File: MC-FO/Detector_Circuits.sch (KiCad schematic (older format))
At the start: 9 parts, among them U16 IFD97, U17 74LVC1G32SE-7, U18 TLV3501AID

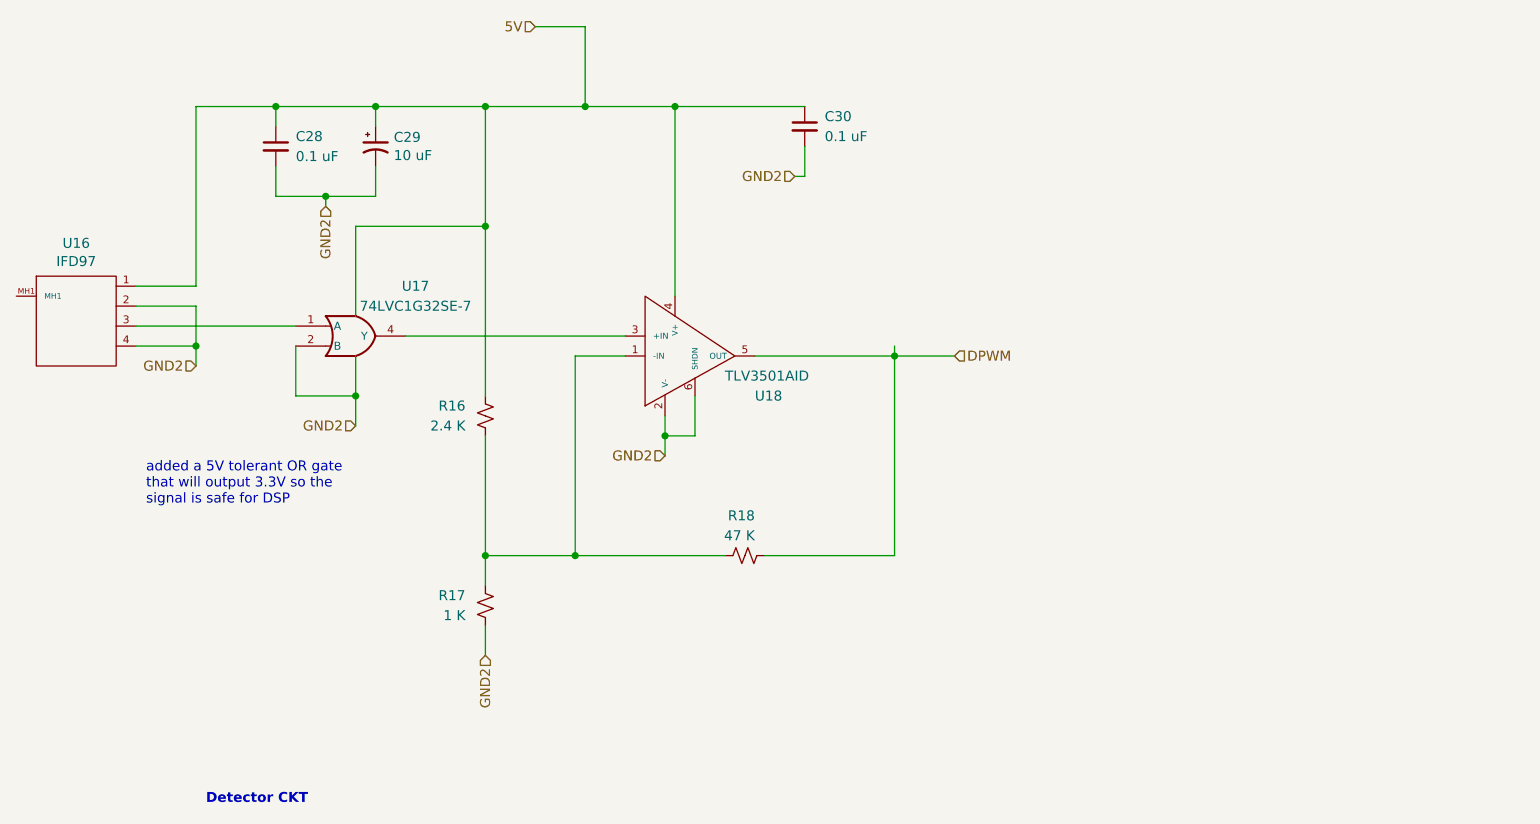
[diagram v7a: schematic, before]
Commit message: unpopulated cap after voltage regulators
and changed reference designator numbering scheme
and moved the or gate that sends 3.3 V to comparator in detector ckt
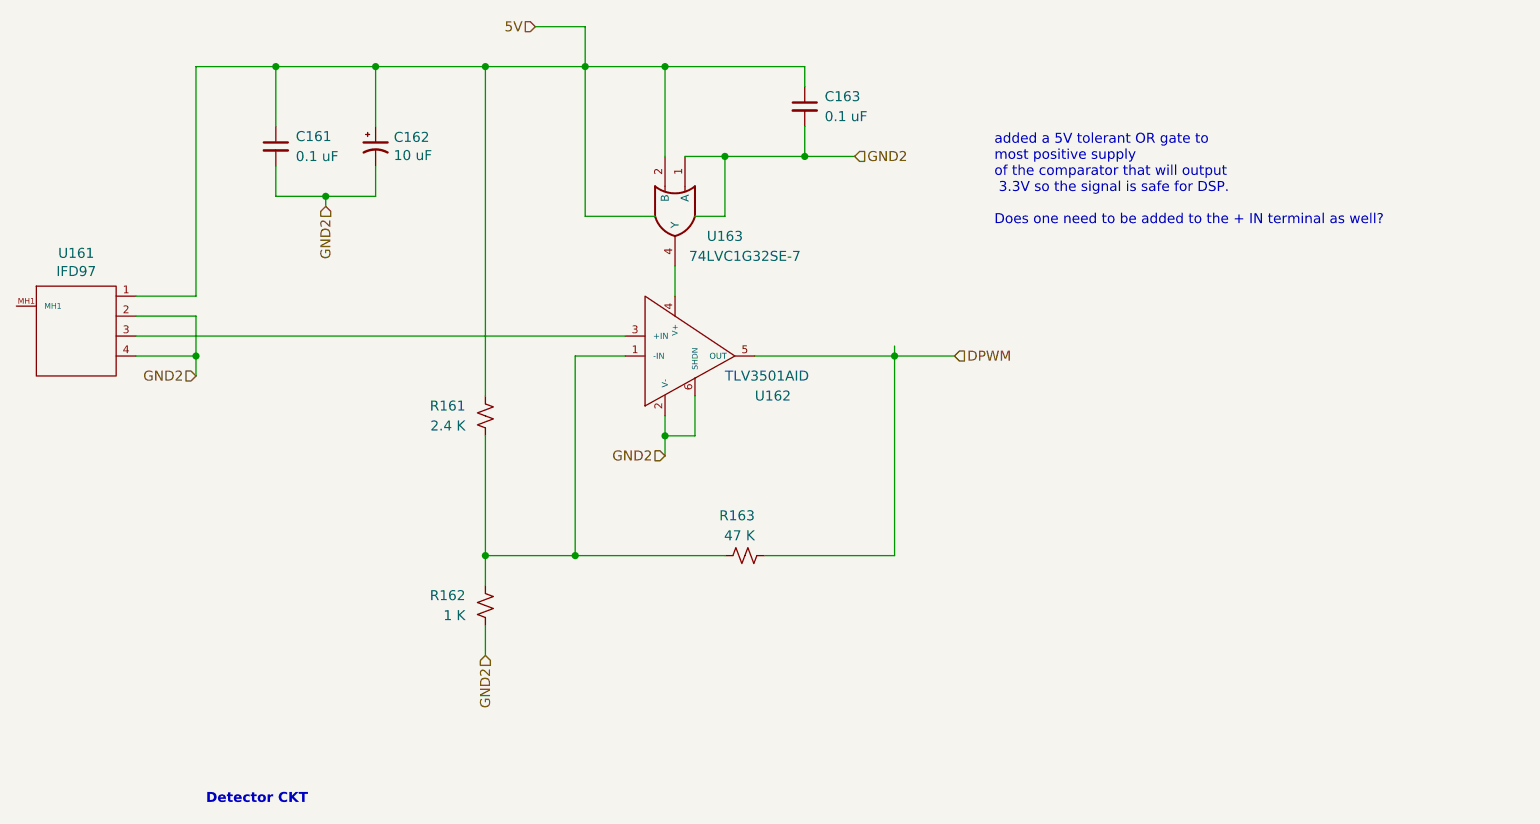
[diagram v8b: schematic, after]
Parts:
- removed U17: 74LVC1G32SE-7, Package_TO_SOT_SMD:SOT-353_SC-70-5_Handsoldering, symbol Existing_IC_Models:74LVC1G32SE-7
- added U143: 74LVC1G32SE-7, Package_TO_SOT_SMD:SOT-353_SC-70-5, symbol Existing_IC_Models:74LVC1G32SE-7
- renumbered C28 to C141, C29 to C142, C30 to C143, R16 to R141, R17 to R142, R18 to R143, U16 to U141, U18 to U142
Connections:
- net GND: now also C141.1, C142.1, C143.1, R141.2, U141.1, U143.2 (B), U143.3 (GND); no longer C141.2, C142.2, C143.2, R142.1, U141.2, U141.4, U142.2 (V-), U142.6 (SHDN)
- net VCC: now also C141.2, C142.2, C143.2, R142.1, U141.2, U141.4, U142.2 (V-), U142.6 (SHDN), U143.1 (A), U143.5 (VCC); no longer C141.1, C142.1, C143.1, R141.2, U141.1, U142.4 (V+)
- net at U142.3 (+IN): now also U141.3
- new net: U142.4 (V+), U143.4 (Y)
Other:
- note added: "added a 5V tolerant OR gate to \nmost positive supply\nof the comparator that will output\n 3.3V so the signal is safe for DSP.\n\nDoes one need to be added to the + IN terminal as well?"
- note removed: "added a 5V tolerant OR gate\nthat will output 3.3V so the\nsignal is safe for DSP"
- moved on the sheet: C163, U161
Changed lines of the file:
@@
 $Descr A4 11693 8268
 encoding utf-8
-Sheet 9 11
+Sheet 8 11
 Title ""
 Date ""
@@
 Detector CKT
 $Comp
-L Device:C_Small C30
+L Device:C_Small C143
 U 1 1 6178E7F5
-P 7350 2500
-AR Path="/6171C819/6178E7F5" Ref="C30"  Part="1"
-AR Path="/61724A08/6178E7F5" Ref="C27"  Part="1"
-F 0 "C30" H 7450 2550 50  0000 L CNN
-F 1 "0.1 uF" H 7450 2450 50  0000 L CNN
-F 2 "Capacitor_SMD:C_0603_1608Metric" H 7350 2500 50  0001 C CNN
-F 3 "~" H 7350 2500 50  0001 C CNN
-	1    7350 2500
-	1    0    0    -1
-$EndComp
-$Comp
-L Device:C_Small C28
+P 7350 2400
+AR Path="/6171C819/6178E7F5" Ref="C143"  Part="1"
+AR Path="/61724A08/6178E7F5" Ref="C163"  Part="1"
+F 0 "C163" H 7450 2450 50  0000 L CNN
+F 1 "0.1 uF" H 7450 2350 50  0000 L CNN
+F 2 "Capacitor_SMD:C_0603_1608Metric" H 7350 2400 50  0001 C CNN
+F 3 "~" H 7350 2400 50  0001 C CNN
+	1    7350 2400
+	1    0    0    -1
+$EndComp
+$Comp
+L Device:C_Small C141
 U 1 1 6178E7F6
 P 4700 2600
-AR Path="/6171C819/6178E7F6" Ref="C28"  Part="1"
-AR Path="/61724A08/6178E7F6" Ref="C25"  Part="1"
-F 0 "C28" H 4800 2650 50  0000 L CNN
+AR Path="/6171C819/6178E7F6" Ref="C141"  Part="1"
+AR Path="/61724A08/6178E7F6" Ref="C161"  Part="1"
+F 0 "C161" H 4800 2650 50  0000 L CNN
 F 1 "0.1 uF" H 4800 2550 50  0000 L CNN
 F 2 "Capacitor_SMD:C_0603_1608Metric" H 4700 2600 50  0001 C CNN
@@
 $EndComp
 $Comp
-L Device:R_Small_US R16
+L Device:R_Small_US R141
 U 1 1 6174EB5A
 P 5750 3950
-AR Path="/6171C819/6174EB5A" Ref="R16"  Part="1"
-AR Path="/61724A08/6174EB5A" Ref="R13"  Part="1"
-F 0 "R16" H 5850 3900 50  0000 L CNN
+AR Path="/6171C819/6174EB5A" Ref="R141"  Part="1"
+AR Path="/61724A08/6174EB5A" Ref="R161"  Part="1"
+F 0 "R161" H 5850 3900 50  0000 L CNN
 F 1 "2.4 K" H 5850 4000 50  0000 L CNN
 F 2 "Resistor_SMD:R_0603_1608Metric" H 5750 3950 50  0001 C CNN
@@
 $EndComp
 $Comp
-L Device:CP1_Small C29
+L Device:CP1_Small C142
 U 1 1 61720E6A
 P 5200 2600
-AR Path="/6171C819/61720E6A" Ref="C29"  Part="1"
-AR Path="/61724A08/61720E6A" Ref="C26"  Part="1"
-F 0 "C29" H 5291 2646 50  0000 L CNN
+AR Path="/6171C819/61720E6A" Ref="C142"  Part="1"
+AR Path="/61724A08/61720E6A" Ref="C162"  Part="1"
+F 0 "C162" H 5291 2646 50  0000 L CNN
 F 1 "10 uF" H 5291 2555 50  0000 L CNN
 F 2 "Capacitor_SMD:C_0603_1608Metric" H 5200 2600 50  0001 C CNN
@@
 	5200 2850 5200 2700
 Wire Wire Line
-	5200 2500 5200 2400
-Connection ~ 5200 2400
-Wire Wire Line
-	4700 2500 4700 2400
-Wire Wire Line
-	4700 2400 5200 2400
+	5200 2500 5200 2200
+Connection ~ 5200 2200
+Wire Wire Line
+	4700 2500 4700 2200
+Wire Wire Line
+	4700 2200 5200 2200
 Wire Wire Line
 	4700 2850 4700 2700
 $Comp
-L Device:R_Small_US R17
+L Device:R_Small_US R142
 U 1 1 617451F8
 P 5750 4900
-AR Path="/6171C819/617451F8" Ref="R17"  Part="1"
-AR Path="/61724A08/617451F8" Ref="R14"  Part="1"
-F 0 "R17" H 5850 4850 50  0000 L CNN
+AR Path="/6171C819/617451F8" Ref="R142"  Part="1"
+AR Path="/61724A08/617451F8" Ref="R162"  Part="1"
+F 0 "R162" H 5850 4850 50  0000 L CNN
 F 1 "1 K" H 5850 4950 50  0000 L CNN
 F 2 "Resistor_SMD:R_0603_1608Metric" H 5750 4900 50  0001 C CNN
@@
 $EndComp
 $Comp
-L Device:R_Small_US R18
+L Device:R_Small_US R143
 U 1 1 61745A42
 P 7050 4650
-AR Path="/6171C819/61745A42" Ref="R18"  Part="1"
-AR Path="/61724A08/61745A42" Ref="R15"  Part="1"
-F 0 "R18" V 7250 4600 50  0000 L CNN
+AR Path="/6171C819/61745A42" Ref="R143"  Part="1"
+AR Path="/61724A08/61745A42" Ref="R163"  Part="1"
+F 0 "R163" V 7250 4600 50  0000 L CNN
 F 1 "47 K" V 7150 4600 50  0000 L CNN
 F 2 "Resistor_SMD:R_0603_1608Metric" H 7050 4650 50  0001 C CNN
@@
 Connection ~ 5750 4650
 Wire Wire Line
-	5750 2400 5750 3000
-Wire Wire Line
-	5200 2400 5750 2400
-Connection ~ 5750 2400
-Wire Wire Line
-	5750 2400 6250 2400
-Wire Wire Line
-	7350 2600 7350 2750
-Wire Wire Line
-	4700 2400 4300 2400
-Wire Wire Line
-	4300 3300 4000 3300
-Connection ~ 4700 2400
-Wire Wire Line
-	4000 3400 4300 3400
-Wire Wire Line
-	4300 3400 4300 3600
-Wire Wire Line
-	4300 3600 4000 3600
-Connection ~ 4300 3600
-Wire Wire Line
-	4300 3600 4300 3700
-Wire Wire Line
-	4300 2400 4300 3300
+	5200 2200 5750 2200
+Connection ~ 5750 2200
+Wire Wire Line
+	5750 2200 6250 2200
+Wire Wire Line
+	4700 2200 4300 2200
+Wire Wire Line
+	4300 3350 4000 3350
+Connection ~ 4700 2200
+Wire Wire Line
+	4000 3450 4300 3450
+Wire Wire Line
+	4300 3450 4300 3650
+Wire Wire Line
+	4300 3650 4000 3650
+Connection ~ 4300 3650
+Wire Wire Line
+	4300 3650 4300 3750
+Wire Wire Line
+	4300 2200 4300 3350
 Wire Wire Line
 	6000 2000 6250 2000
 Wire Wire Line
-	6250 2000 6250 2400
-Connection ~ 6250 2400
-Wire Wire Line
-	6250 2400 6700 2400
-Wire Wire Line
-	6700 3350 6700 2400
-Connection ~ 6700 2400
-Wire Wire Line
-	6700 2400 7350 2400
+	6250 2000 6250 2200
+Connection ~ 6250 2200
+Wire Wire Line
+	6700 3350 6700 3200
 Connection ~ 6200 4650
 Wire Wire Line
@@
 	7100 3650 7800 3650
 $Comp
-L Existing_IC_Models:IFD97 U16
+L Existing_IC_Models:IFD97 U141
 U 1 1 61758365
-P 3700 3900
-AR Path="/6171C819/61758365" Ref="U16"  Part="1"
-AR Path="/61724A08/61758365" Ref="U13"  Part="1"
-F 0 "U16" H 3700 4715 50  0000 C CNN
-F 1 "IFD97" H 3700 4624 50  0000 C CNN
-F 2 "Footprints_MC-FO:IFD97" H 3700 4700 50  0001 C CNN
-F 3 "" H 3700 4700 50  0001 C CNN
-	1    3700 3900
+P 3700 3950
+AR Path="/6171C819/61758365" Ref="U141"  Part="1"
+AR Path="/61724A08/61758365" Ref="U161"  Part="1"
+F 0 "U161" H 3700 4765 50  0000 C CNN
+F 1 "IFD97" H 3700 4674 50  0000 C CNN
+F 2 "Footprints_MC-FO:IFD97" H 3700 4750 50  0001 C CNN
+F 3 "" H 3700 4750 50  0001 C CNN
+	1    3700 3950
 	1    0    0    -1
 $EndComp
@@
 5V
 $Comp
-L Existing_IC_Models:TLV3501AID U18
+L Existing_IC_Models:TLV3501AID U142
 U 1 1 61744BAA
 P 6600 3950
-AR Path="/6171C819/61744BAA" Ref="U18"  Part="1"
-AR Path="/61724A08/61744BAA" Ref="U15"  Part="1"
-F 0 "U18" H 7100 3850 50  0000 L CNN
+AR Path="/6171C819/61744BAA" Ref="U142"  Part="1"
+AR Path="/61724A08/61744BAA" Ref="U162"  Part="1"
+F 0 "U162" H 7100 3850 50  0000 L CNN
 F 1 "TLV3501AID" H 6950 3750 50  0000 L CNN
 F 2 "Package_SO:SOIC-8_3.9x4.9mm_P1.27mm" H 6600 3950 50  0001 C CNN
@@
 Text HLabel 5750 5150 3    50   Input ~ 0
 GND2
-$Comp
-L Existing_IC_Models:74LVC1G32SE-7 U17
-U 1 1 6177D138
-P 5100 3550
-AR Path="/6171C819/6177D138" Ref="U17"  Part="1"
-AR Path="/61724A08/6177D138" Ref="U14"  Part="1"
-F 0 "U17" H 5400 3800 50  0000 C CNN
-F 1 "74LVC1G32SE-7" H 5400 3700 50  0000 C CNN
-F 2 "Package_TO_SOT_SMD:SOT-353_SC-70-5_Handsoldering" H 5100 3550 50  0001 C CNN
-F 3 "http://www.ti.com/lit/sg/scyt129e/scyt129e.pdf" H 5100 3550 50  0001 C CNN
-	1    5100 3550
-	1    0    0    -1
-$EndComp
-Wire Wire Line
-	4000 3500 4800 3500
-Wire Wire Line
-	5100 3650 5100 3850
-Wire Wire Line
-	5100 3850 4800 3850
-Wire Wire Line
-	4800 3850 4800 3600
-Wire Wire Line
-	5100 3850 5100 4000
-Connection ~ 5100 3850
-Text HLabel 5100 4000 0    50   Input ~ 0
-GND2
-Wire Wire Line
-	5350 3550 6450 3550
 Text HLabel 6650 4150 0    50   Input ~ 0
 GND2
-Wire Wire Line
-	5750 3000 5100 3000
-Wire Wire Line
-	5100 3000 5100 3450
-Connection ~ 5750 3000
-Wire Wire Line
-	5750 3000 5750 3850
 Text HLabel 4950 2900 3    50   Input ~ 0
 GND2
-Text HLabel 4300 3700 0    50   Input ~ 0
-GND2
-Text HLabel 7300 2750 0    50   Input ~ 0
-GND2
-Wire Wire Line
-	7300 2750 7350 2750
-Text Notes 4050 4400 0    50   ~ 0
-added a 5V tolerant OR gate\nthat will output 3.3V so the\nsignal is safe for DSP
+Text HLabel 4300 3750 0    50   Input ~ 0
+GND2
+Text HLabel 7600 2650 2    50   Input ~ 0
+GND2
+Text Notes 8300 3000 0    50   ~ 0
+added a 5V tolerant OR gate to \nmost positive supply\nof the comparator that will output\n 3.3V so the signal is safe for DSP.\n\nDoes one need to be added to the + IN terminal as well?
 Wire Wire Line
 	4700 2850 4950 2850
@@
 Wire Wire Line
 	4950 2850 5200 2850
+$Comp
+L Existing_IC_Models:74LVC1G32SE-7 U143
+U 1 1 617F3635
+P 6700 2950
+AR Path="/6171C819/617F3635" Ref="U143"  Part="1"
+AR Path="/61724A08/617F3635" Ref="U163"  Part="1"
+F 0 "U163" V 6800 3200 50  0000 C CNN
+F 1 "74LVC1G32SE-7" V 6900 3300 50  0000 C CNN
+F 2 "Package_TO_SOT_SMD:SOT-353_SC-70-5" H 6700 2950 50  0001 C CNN
+F 3 "http://www.ti.com/lit/sg/scyt129e/scyt129e.pdf" H 6700 2950 50  0001 C CNN
+	1    6700 2950
+	0    1    1    0
+$EndComp
+Wire Wire Line
+	6250 2200 6650 2200
+Wire Wire Line
+	6650 2200 6650 2650
+Connection ~ 6650 2200
+Wire Wire Line
+	6650 2200 7350 2200
+Wire Wire Line
+	6600 2950 6250 2950
+Wire Wire Line
+	6250 2950 6250 2200
+Wire Wire Line
+	6750 2650 6950 2650
+Wire Wire Line
+	6800 2950 6950 2950
+Wire Wire Line
+	6950 2950 6950 2650
+Connection ~ 6950 2650
+Wire Wire Line
+	6950 2650 7350 2650
+Wire Wire Line
+	7350 2500 7350 2650
+Wire Wire Line
+	7350 2200 7350 2300
+Wire Wire Line
+	7350 2650 7600 2650
+Connection ~ 7350 2650
+Wire Wire Line
+	5750 2200 5750 3850
+Wire Wire Line
+	4000 3550 6450 3550
 $EndSCHEMATC
